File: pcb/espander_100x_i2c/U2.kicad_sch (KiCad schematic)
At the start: 5 parts, among them J1 DG127A-5.08-06P-14-00AH, J2 DG127A-5.08-06P-14-00AH, J3 DG127A-5.08-06P-14-00AH, J4 DG127A-5.08-06P-14-00AH, U1 MCP23017_SP

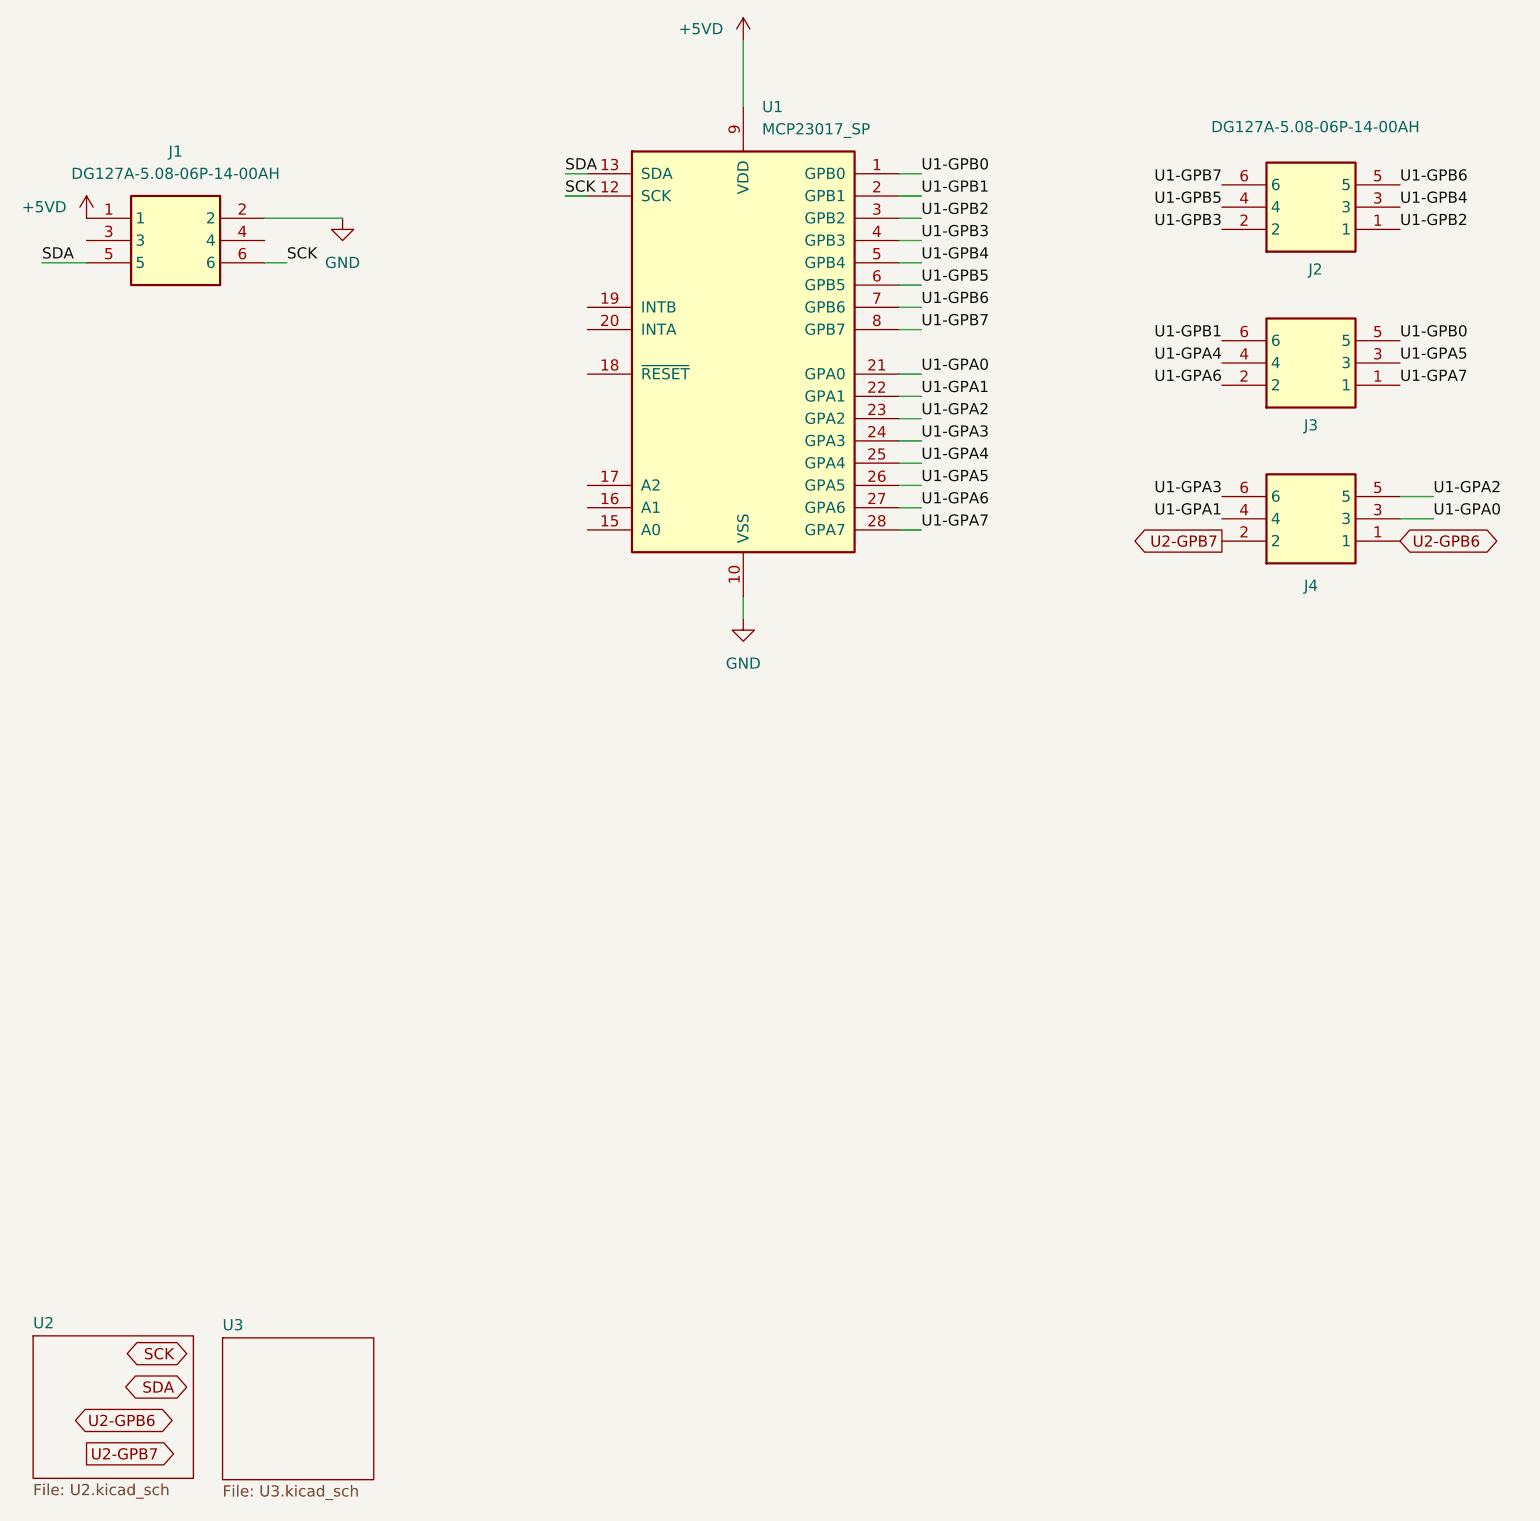
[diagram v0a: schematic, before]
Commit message: Add initial DRU file for espander_100x_i2c PCB design
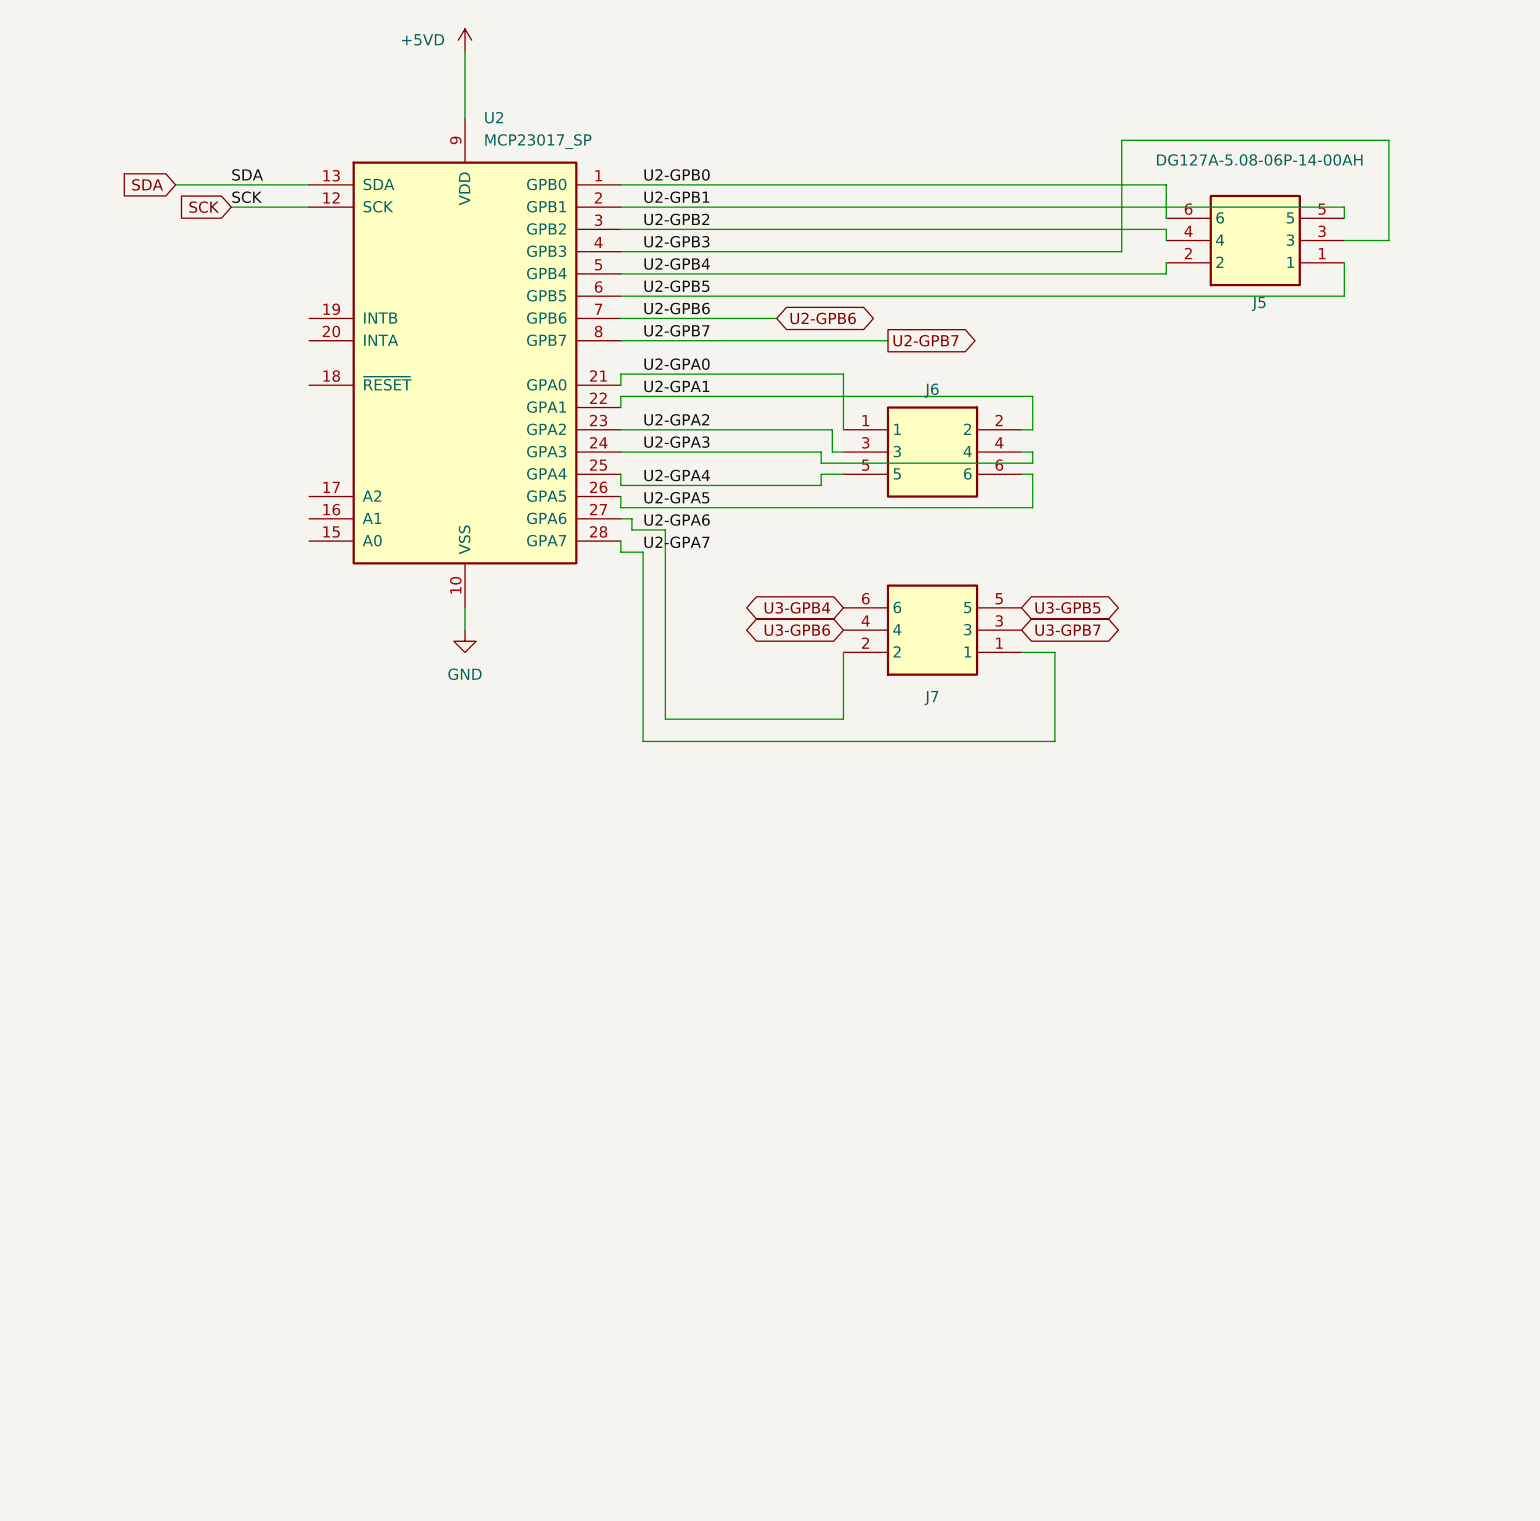
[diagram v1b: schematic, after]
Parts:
- removed J1, J2, J3, J4: DG127A-5.08-06P-14-00AH, DG127A50806P1400AH, symbol 1_tme:DG127A-5.08-06P-14-00AH
- removed U1: MCP23017_SP, Package_DIP:DIP-28_W7.62mm, symbol Interface_Expansion:MCP23017_SP
- added J5, J6, J7: DG127A-5.08-06P-14-00AH, DG127A50806P1400AH, symbol 1_tme:DG127A-5.08-06P-14-00AH
- added U2: MCP23017_SP, Package_DIP:DIP-28_W7.62mm, symbol Interface_Expansion:MCP23017_SP
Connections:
- net +5VD: now also U2.9 (VDD)
- net GND: now also U2.10 (VSS)
- net SCK: now also U2.12 (SCK)
- net SDA: now also U2.13 (SDA)
- net U2-GPB6: now also U2.7 (GPB6)
- net U2-GPB7: now also U2.8 (GPB7)
- new net U2-GPA0: J6.1, U2.21 (GPA0)
- new net U2-GPA1: J6.2, U2.22 (GPA1)
- new net U2-GPA2: J6.3, U2.23 (GPA2)
- new net U2-GPA3: J6.4, U2.24 (GPA3)
- new net U2-GPA4: J6.5, U2.25 (GPA4)
- new net U2-GPA5: J6.6, U2.26 (GPA5)
- new net U2-GPA6: J7.2, U2.27 (GPA6)
- new net U2-GPA7: J7.1, U2.28 (GPA7)
- new net U2-GPB0: J5.6, U2.1 (GPB0)
- new net U2-GPB1: J5.5, U2.2 (GPB1)
- new net U2-GPB2: J5.4, U2.3 (GPB2)
- new net U2-GPB3: J5.3, U2.4 (GPB3)
- new net U2-GPB4: J5.2, U2.5 (GPB4)
- new net U2-GPB5: J5.1, U2.6 (GPB5)
- new net U3-GPB4: J7.6
- new net U3-GPB5: J7.5
- new net U3-GPB6: J7.4
- new net U3-GPB7: J7.3
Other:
- removed sheet U2
- removed sheet U3

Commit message: Refactor code structure for improved readability and maintainability
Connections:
- net U2-GPA0: now also J6.6; no longer J6.1
- net U2-GPA1: now also J6.5; no longer J6.2
- net U2-GPA2: now also J7.5; no longer J6.3
- net U2-GPA3: now also J7.6; no longer J6.4
- net U2-GPA4: now also J6.1; no longer J6.5
- net U2-GPA5: now also J6.2; no longer J6.6
- net U2-GPA6: now also J6.3; no longer J7.2
- net U2-GPA7: now also J6.4; no longer J7.1
- net U2-GPB0: now also J5.1; no longer J5.6
- net U2-GPB1: now also J5.2; no longer J5.5
- net U2-GPB2: now also J5.3; no longer J5.4
- net U2-GPB3: now also J5.4; no longer J5.3
- net U2-GPB4: now also J5.5; no longer J5.2
- net U2-GPB5: now also J5.6; no longer J5.1
- net U3-GPB4: no longer J7.6
- net U3-GPB5: no longer J7.5
- net U3-GPB6: no longer J7.4
- net U3-GPB7: no longer J7.3
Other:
- moved on the sheet: J6

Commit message: RESYNC
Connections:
- net U3-GPB4: now also J7.1
- net U3-GPB5: now also J7.2
- net U3-GPB6: now also J7.3
- net U3-GPB7: now also J7.4
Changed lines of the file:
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@@
 	(global_label "U3-GPB6"
 		(shape bidirectional)
-		(at 102.87 116.84 180)
+		(at 130.81 97.79 0)
 		(fields_autoplaced yes)
 		(effects
@@
 				(size 1.27 1.27)
 			)
-			(justify right)
+			(justify left)
 		)
 		(property "Intersheetrefs" "${INTERSHEET_REFS}"
-			(at 89.6416 116.84 0)
+			(at 144.0384 97.79 0)
 			(effects
 				(font
 					(size 1.27 1.27)
 				)
-				(justify right)
+				(justify left)
 				(hide yes)
 			)
@@
 	(global_label "U3-GPB4"
 		(shape bidirectional)
-		(at 102.87 114.3 180)
+		(at 130.81 100.33 0)
 		(fields_autoplaced yes)
 		(effects
@@
 				(size 1.27 1.27)
 			)
-			(justify right)
+			(justify left)
 		)
 		(property "Intersheetrefs" "${INTERSHEET_REFS}"
-			(at 89.6416 114.3 0)
+			(at 144.0384 100.33 0)
 			(effects
 				(font
 					(size 1.27 1.27)
 				)
-				(justify right)
+				(justify left)
 				(hide yes)
 			)
@@
 	(global_label "U3-GPB5"
 		(shape bidirectional)
-		(at 138.43 106.68 0)
+		(at 110.49 100.33 180)
 		(fields_autoplaced yes)
 		(effects
@@
 				(size 1.27 1.27)
 			)
-			(justify left)
+			(justify right)
 		)
 		(property "Intersheetrefs" "${INTERSHEET_REFS}"
-			(at 151.6584 106.68 0)
+			(at 97.2616 100.33 0)
 			(effects
 				(font
 					(size 1.27 1.27)
 				)
-				(justify left)
+				(justify right)
 				(hide yes)
 			)
@@
 	(global_label "U3-GPB7"
 		(shape bidirectional)
-		(at 138.43 109.22 0)
+		(at 110.49 97.79 180)
 		(fields_autoplaced yes)
 		(effects
@@
 				(size 1.27 1.27)
 			)
-			(justify left)
+			(justify right)
 		)
 		(property "Intersheetrefs" "${INTERSHEET_REFS}"
-			(at 151.6584 109.22 0)
+			(at 97.2616 97.79 0)
 			(effects
 				(font
 					(size 1.27 1.27)
 				)
-				(justify left)
+				(justify right)
 				(hide yes)
 			)

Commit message: resync
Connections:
- net U2-GPA0: no longer J6.6
- net U2-GPA1: no longer J6.5
- net U2-GPA2: no longer J7.5
- net U2-GPA3: no longer J7.6
- net U2-GPA4: no longer J6.1
- net U2-GPA5: no longer J6.2
- net U2-GPA6: no longer J6.3
- net U2-GPA7: no longer J6.4
- net U2-GPB0: no longer J5.1
- net U2-GPB1: no longer J5.2
- net U2-GPB2: no longer J5.3
- net U2-GPB3: no longer J5.4
- net U2-GPB4: no longer J5.5
- net U2-GPB5: no longer J5.6
- net U3-GPB4: no longer names the net of J7.1
- net U3-GPB5: no longer names the net of J7.2
- net U3-GPB6: no longer names the net of J7.3
- net U3-GPB7: no longer names the net of J7.4

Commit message: ekspander resync
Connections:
- net +5VD renamed +3V3
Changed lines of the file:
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@@
 			)
 		)
-		(property "Value" "+5VD"
+		(property "Value" "+3V3"
 			(at 62.484 30.48 0)
 			(effects
